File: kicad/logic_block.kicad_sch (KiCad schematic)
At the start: 50 parts, among them U201 TBD62083AFNG, U202 MCP23S17T-E/SS, U203 TBD62083AFNG

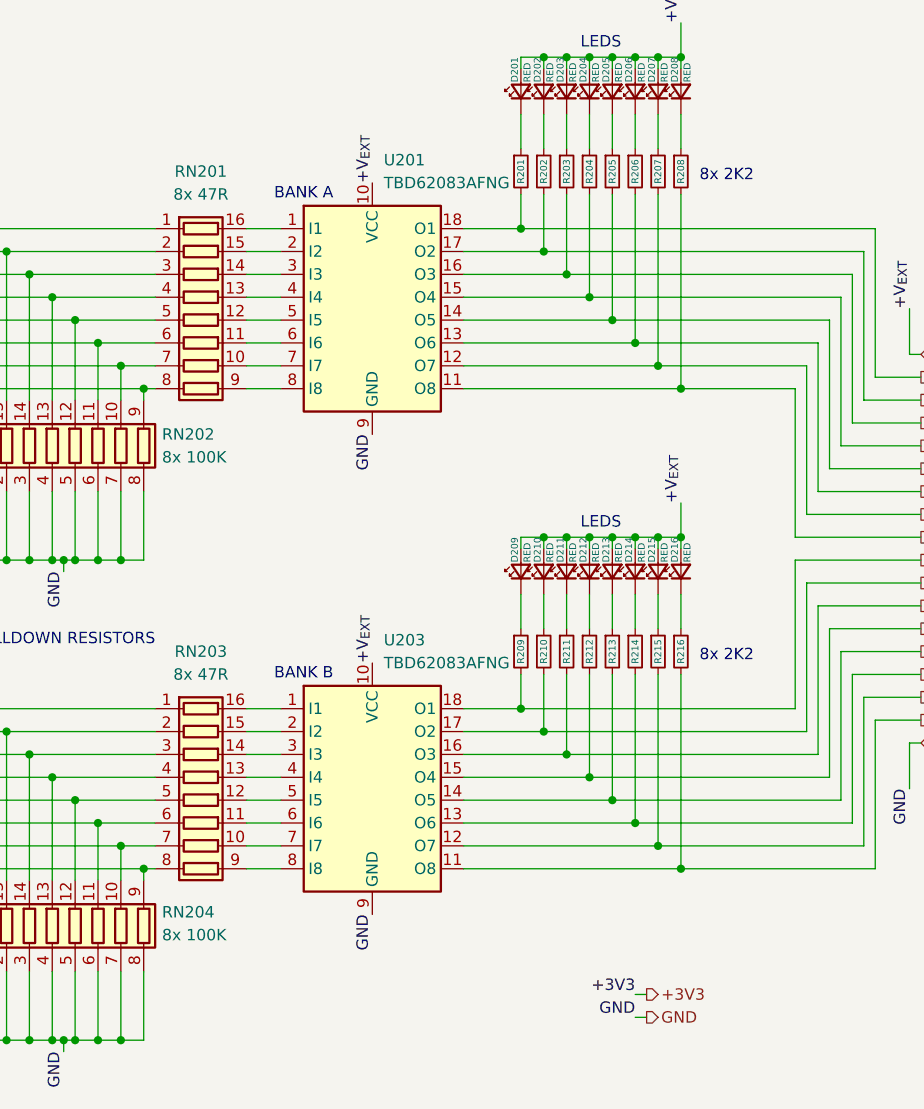
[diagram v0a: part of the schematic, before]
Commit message: feat: add LCSC parts numbers
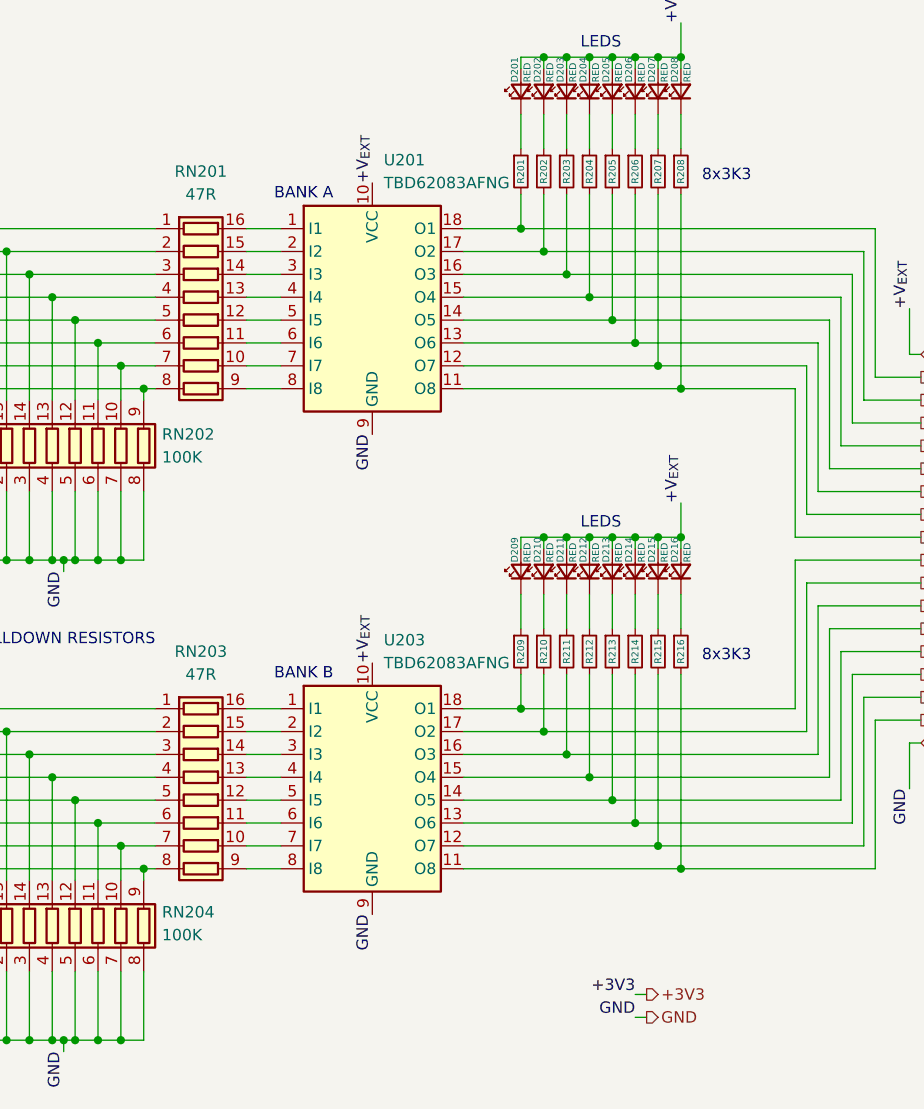
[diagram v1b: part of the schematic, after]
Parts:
- C201, C204, C206, C208: LCSC# (none) -> C161115; Mouser Part Number 81-GCJ188R71H104KA2D -> (none); Mouser# (none) -> 81-GCJ188R71H104KA2D
- C202: LCSC# (none) -> C445456; Mouser Part Number 647-UCM1J101MNL1GS -> (none); Mouser# (none) -> 647-UCM1J101MNL1GS
- C203: LCSC# (none) -> C668370; Mouser Part Number 81-GRT188R61H225KE3D -> (none); Mouser# (none) -> 81-GRT188R61H225KE3D
- C205, C207: LCSC# (none) -> C126631; Mouser Part Number 81-GRT188R61H105KE3D -> (none); Mouser# (none) -> 81-GRT188R61H105KE3D
- D201, D202, D203, D204, D205, D206, D207, D208, D209, D210, D211, D212, D213, D214, D215, D216: LCSC# (none) -> C364560; Mouser Part Number 859-LTST-C190EKT -> (none); Mouser# (none) -> 859-LTST-C190EKT
- D217: LCSC# (none) -> C720171; Mouser Part Number 576-SMBJ45A -> (none); Mouser# (none) -> 576-SMBJ45A
- R201, R202, R203, R204, R205, R206, R207, R208, R209, R210, R211, R212, R213, R214, R215, R216: value 10K -> 3K3; LCSC# (none) -> C491202; Mouser Part Number 667-ERJ-UP3J103V -> (none); Mouser# (none) -> 667-ERJ-UP3J332V; Part Number ERJ-UP3J103V -> ERJ-UP3J332V
- R217: LCSC# (none) -> C4297913; Mouser Part Number 667-ERJ-H3EF1002V -> (none); Mouser# (none) -> 667-ERJ-H3EF1002V
- R218: LCSC# (none) -> C4313361; Mouser Part Number 667-ERJ-H3EF33R0V -> (none); Mouser# (none) -> 667-ERJ-H3EF33R0V
- RN201, RN203: value 8x 47R -> 47R; LCSC# (none) -> C713462; Mouser Part Number 667-EXB-2HV470JV -> (none); Mouser# (none) -> 667-EXB-2HV470JV
- RN202, RN204: value 8x 100K -> 100K; LCSC# (none) -> C713455; Mouser Part Number 667-EXB-2HV104JV -> (none); Mouser# (none) -> 667-EXB-2HV104JV
- U201, U203: LCSC# (none) -> C163229; Mouser Part Number 757-TBD62083AFNGEL -> (none); Mouser# (none) -> 757-TBD62083AFNGEL
- U202: LCSC# (none) -> C128577; Mouser Part Number 579-MCP23S17T-E/SS -> (none); Mouser# (none) -> 579-MCP23S17T-E/SS
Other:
- note added: "8x3K3"
- note removed: "8x 2K2"
